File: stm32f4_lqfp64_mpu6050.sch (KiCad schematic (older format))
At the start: 65 parts, among them M1 ALIS-CUSTOM-PARTS_POWERPADS, M2 ALIS-CUSTOM-PARTS_POWERPADS, M3 ALIS-CUSTOM-PARTS_POWERPADS, M4 ALIS-CUSTOM-PARTS_POWERPADS, M5 ALIS-CUSTOM-PARTS_POWERPADS, Q1 CRYSTAL_50X32, Q2 BSS138, Q3 BSS138, Q4 BSS138, Q5 BSS138, Q6 BSS138, U1 STM32_STM32F10XRXT6, U2 MPU6050, U3 LP2985LV, U4 ublox_neo7, X1 CON-JST_SM04B-SRSS-TB, X2 CON-JST_SM04B-SRSS-TB, X3 CON-JST_SM04B-SRSS-TB, X4 CON-JST_SM04B-SRSS-TB, X5 CON-JST_SM04B-SRSS-TB, X6 CON-JST_SM04B-SRSS-TB, X7 CON-JST_SM04B-SRSS-TB, X8 CON-JST_SM04B-SRSS-TB

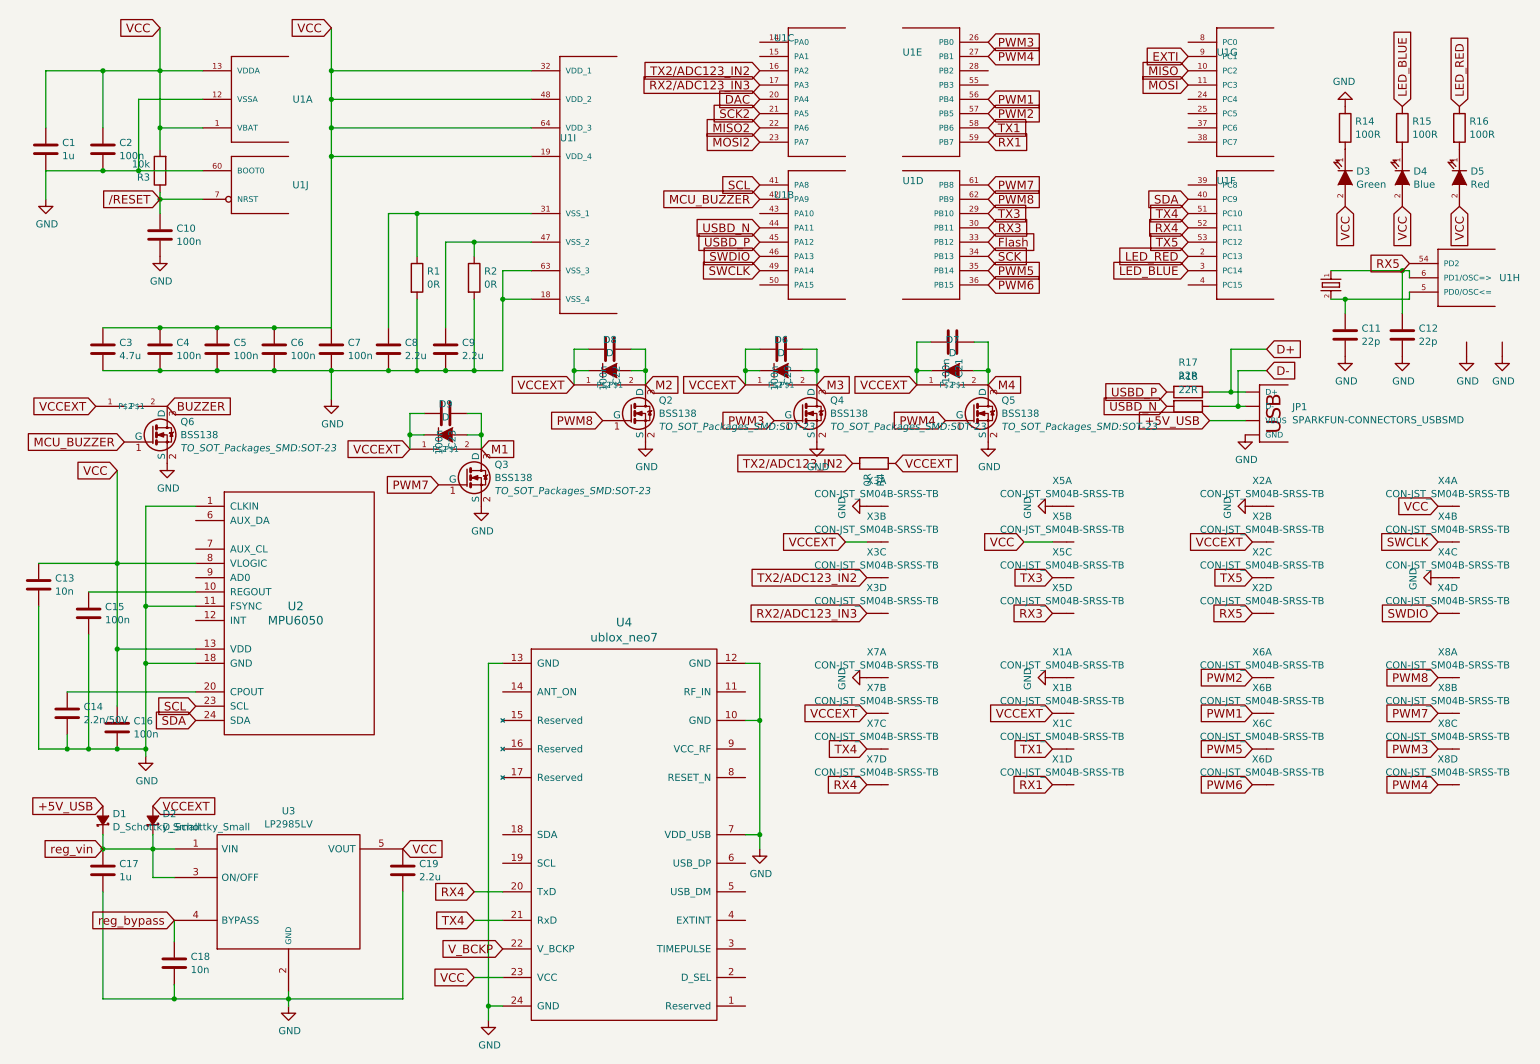
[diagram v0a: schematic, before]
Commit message: moved schematic blocks to hierarchical sheets
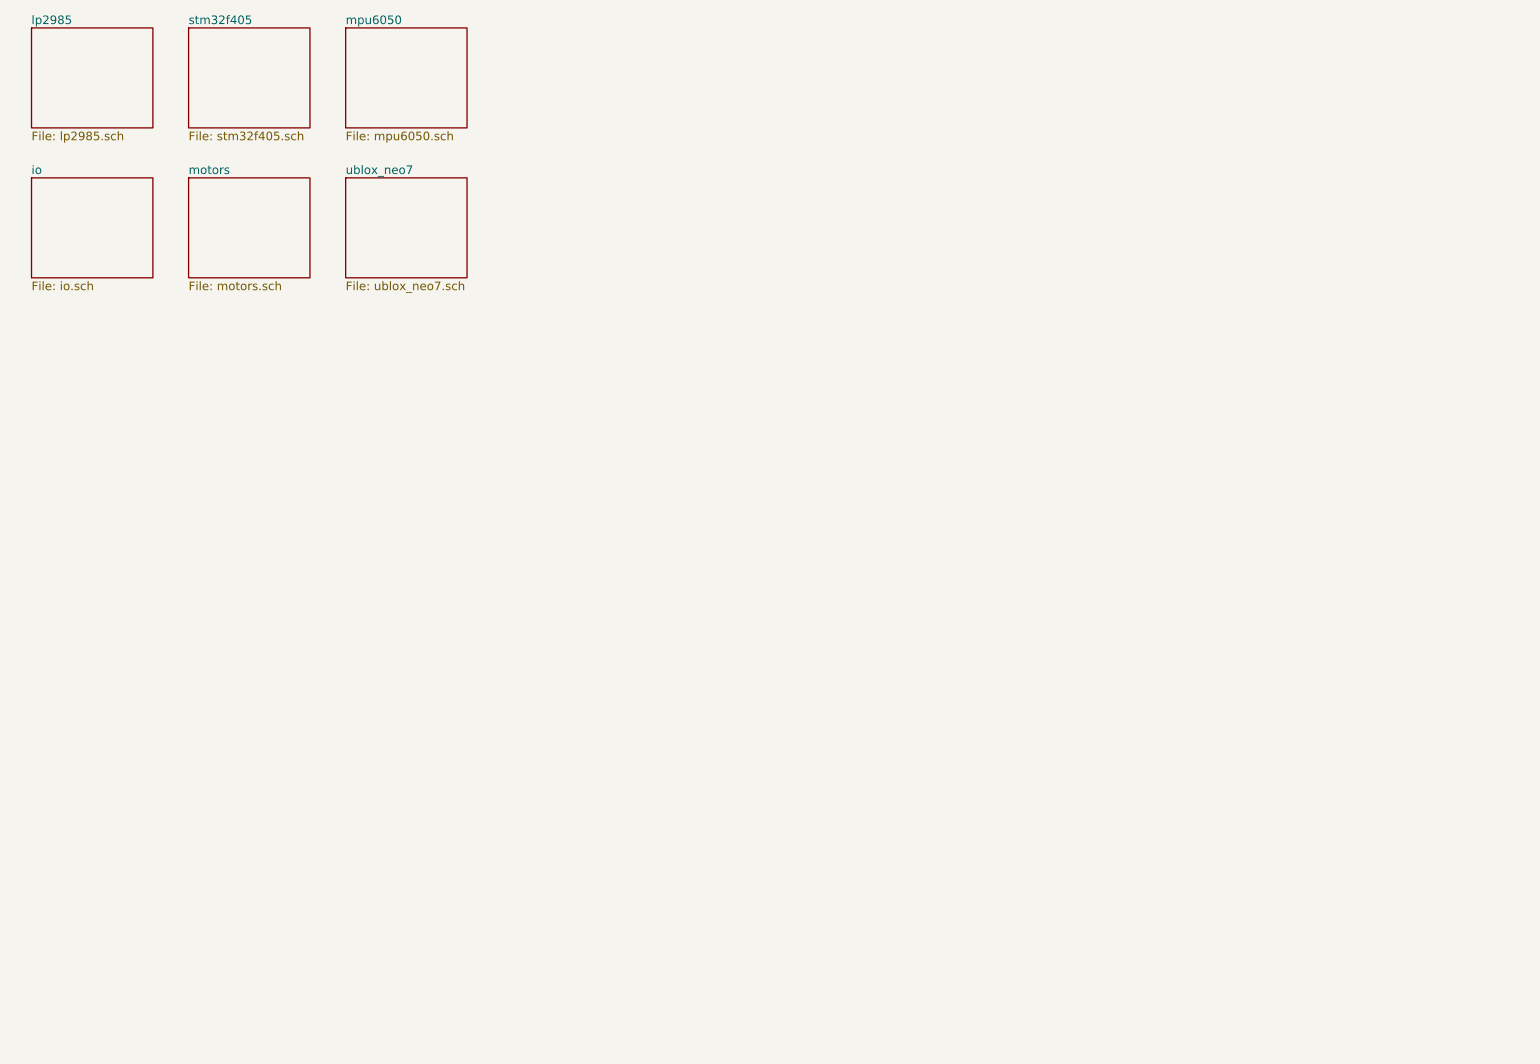
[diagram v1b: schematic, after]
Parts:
- removed C1, C17: 1u, Capacitors_SMD:C_0402, symbol C
- removed C10, C15, C16, C2, C20, C21, C22, C23, C4, C5, C6, C7: 100n, Capacitors_SMD:C_0402, symbol C
- removed C11, C12: 22p, Capacitors_SMD:C_0402, symbol C
- removed C13, C18: 10n, Capacitors_SMD:C_0402, symbol C
- removed C14: 2.2n/50V, Capacitors_SMD:C_0603, symbol C
- removed C19, C8, C9: 2.2u, Capacitors_SMD:C_0603, symbol C
- removed C3: 4.7u, Capacitors_SMD:C_0805, symbol C
- removed D1, D2: D_Schottky_Small, Diodes_SMD:SMA_Standard, symbol D_Schottky_Small
- removed D3: Green, LEDs:LED-0805, symbol LED
- removed D4: Blue, LEDs:LED-0805, symbol LED
- removed D5: Red, LEDs:LED-0805, symbol LED
- removed D6, D7, D8, D9: D, Diodes_SMD:SMA_Standard, symbol D
- removed JP1: SPARKFUN-CONNECTORS_USBSMD, minimal:SPARKFUN-CONNECTORS_USB-MINIB, symbol SPARKFUN-CONNECTORS_USBSMD
- removed M1, M2, M3, M4, M5: ALIS-CUSTOM-PARTS_POWERPADS, minimal:ALIS-CUSTOM-PARTS_PAD-JUMPER-2-NO_YES_SILK, symbol ALIS-CUSTOM-PARTS_POWERPADS
- removed Q1: CRYSTAL_50X32, minimal:CRYSTAL_50X32, symbol CRYSTAL_50X32
- removed Q2, Q3, Q4, Q5, Q6: BSS138, TO_SOT_Packages_SMD:SOT-23, symbol BSS138
- removed R1, R2, R4: 0R, Resistors_SMD:R_0402, symbol R
- removed R14, R15, R16: 100R, Resistors_SMD:R_0402, symbol R
- removed R17, R18: 22R, Resistors_SMD:R_0402, symbol R
- removed R3: 10k, Resistors_SMD:R_0402, symbol R
- removed U1: STM32_STM32F10XRXT6, Housings_QFP:LQFP-64_10x10mm_Pitch0.5mm, symbol STM32_STM32F10XRXT6
- removed U2: MPU6050, Housings_DFN_QFN:QFN-24-1EP_4x4mm_Pitch0.5mm, symbol MPU6050
- removed U3: LP2985LV, TO_SOT_Packages_SMD:SOT-23-5, symbol LP2985LV
- removed U4: ublox_neo7, alis_parts:ublox_neo7, symbol ublox_neo7
- removed X1, X2, X3, X4, X5, X6, X7, X8: CON-JST_SM04B-SRSS-TB, Connectors_JST_SH:Connectors_JST_SM04B-SRSS-TB, symbol CON-JST_SM04B-SRSS-TB
